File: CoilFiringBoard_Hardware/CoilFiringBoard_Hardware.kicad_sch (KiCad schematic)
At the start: 21 parts, among them Q1 Q_NMOS_GDS, Q2 Q_NMOS_GDS

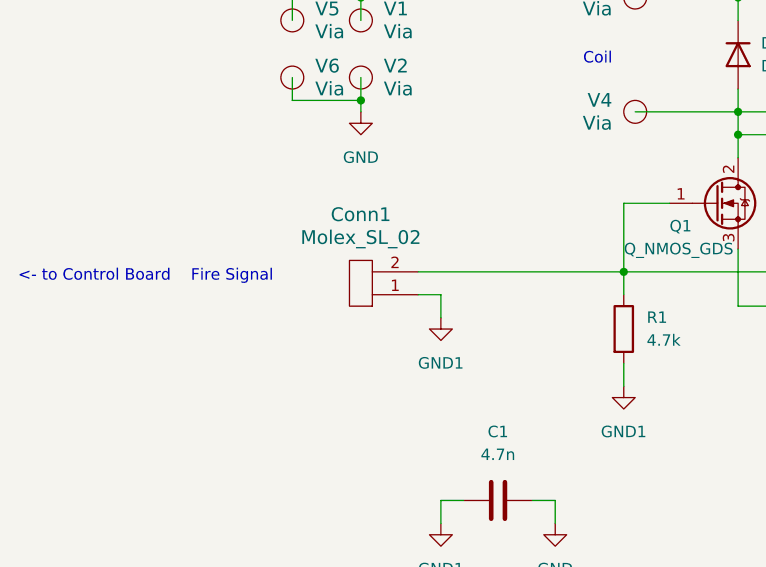
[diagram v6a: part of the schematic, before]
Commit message: Adjusted gate traces
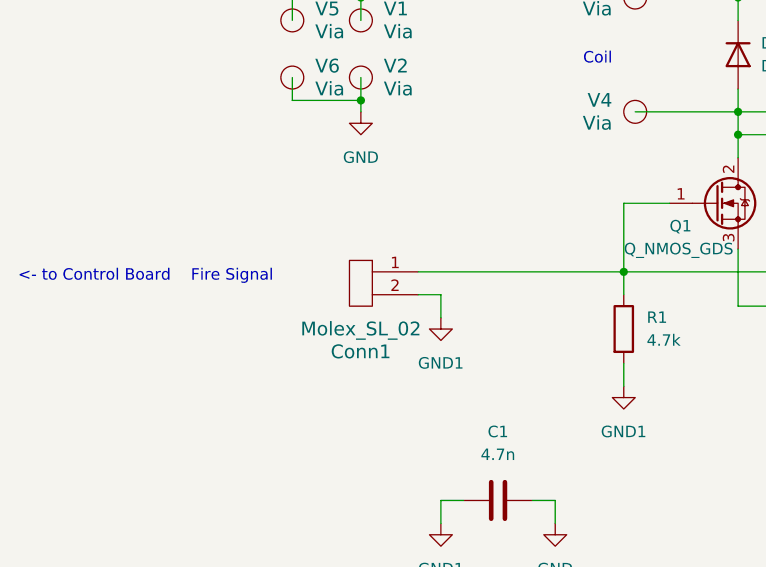
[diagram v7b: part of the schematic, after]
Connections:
- net GND1: now also Conn1.2; no longer Conn1.1
- net at Q1.1 (G), Q2.1 (G), R1.1: now also Conn1.1; no longer Conn1.2
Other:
- moved on the sheet: Conn1
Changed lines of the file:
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@@
     )
   )
-  (symbol (lib_id "MRDT_Connectors:Molex_SL_02") (at 105.41 90.17 180) (unit 1)
-    (in_bom yes) (on_board yes) (dnp no) (fields_autoplaced)
-    (property "Reference" "Conn1" (at 104.14 85.09 0)
+  (symbol (lib_id "MRDT_Connectors:Molex_SL_02") (at 105.41 95.25 0) (mirror y) (unit 1)
+    (in_bom yes) (on_board yes) (dnp no)
+    (property "Reference" "Conn1" (at 104.14 100.33 0)
       (effects (font (size 1.524 1.524)))
     )
-    (property "Value" "Molex_SL_02" (at 104.14 87.63 0)
+    (property "Value" "Molex_SL_02" (at 104.14 97.79 0)
       (effects (font (size 1.524 1.524)))
     )
-    (property "Footprint" "MRDT_Connectors:MOLEX_SL_02_Horizontal" (at 105.41 87.63 0)
+    (property "Footprint" "MRDT_Connectors:MOLEX_SL_02_Horizontal" (at 105.41 97.79 0)
       (effects (font (size 1.524 1.524)) hide)
     )
-    (property "Datasheet" "" (at 105.41 87.63 0)
+    (property "Datasheet" "" (at 105.41 97.79 0)
       (effects (font (size 1.524 1.524)) hide)
     )

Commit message: Updated schematic
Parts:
- removed D10, D5, D6, D7, D8, D9: D, Diode_THT:D_DO-15_P12.70mm_Horizontal, symbol Device:D
- added R2: 4.7k, Resistor_SMD:R_0603_1608Metric_Pad0.98x0.95mm_HandSolder, symbol Device:R
- C1: footprint Capacitor_THT:CP_Radial_D10.0mm_P5.00mm -> Capacitor_THT:C_Disc_D10.5mm_W5.0mm_P10.00mm
- D1, D2, D3, D4: footprint Diode_THT:D_DO-15_P12.70mm_Horizontal -> Diode_THT:D_DO-201AD_P12.70mm_Horizontal
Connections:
- net GND1: now also R2.2
- net at Conn1.1, Q1.1 (G), Q2.1 (G)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: now also R2.1
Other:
- moved on the sheet: R1
